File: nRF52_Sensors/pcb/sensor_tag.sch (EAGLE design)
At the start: 6 parts

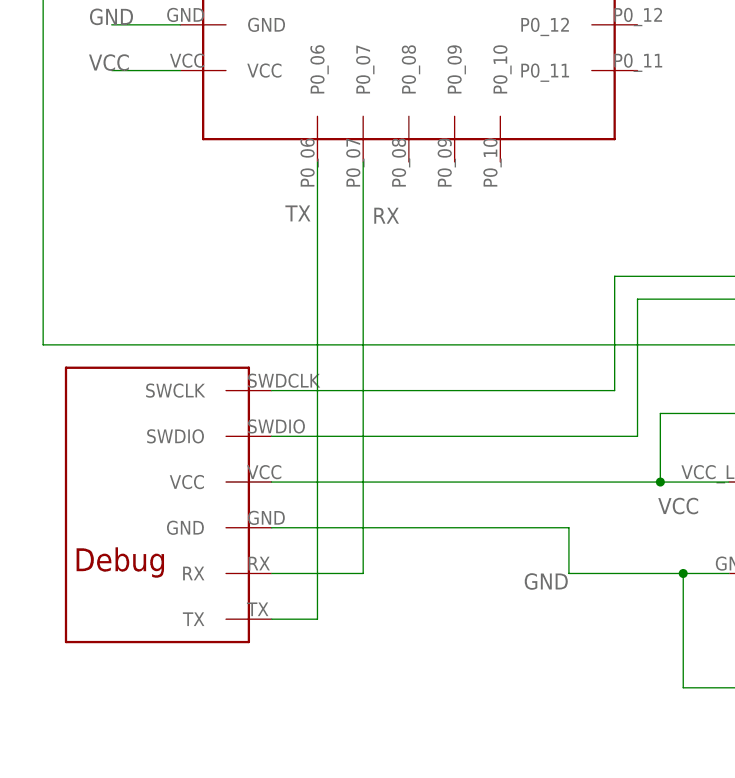
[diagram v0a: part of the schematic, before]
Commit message: fixed board design issues and zip gerber of new order
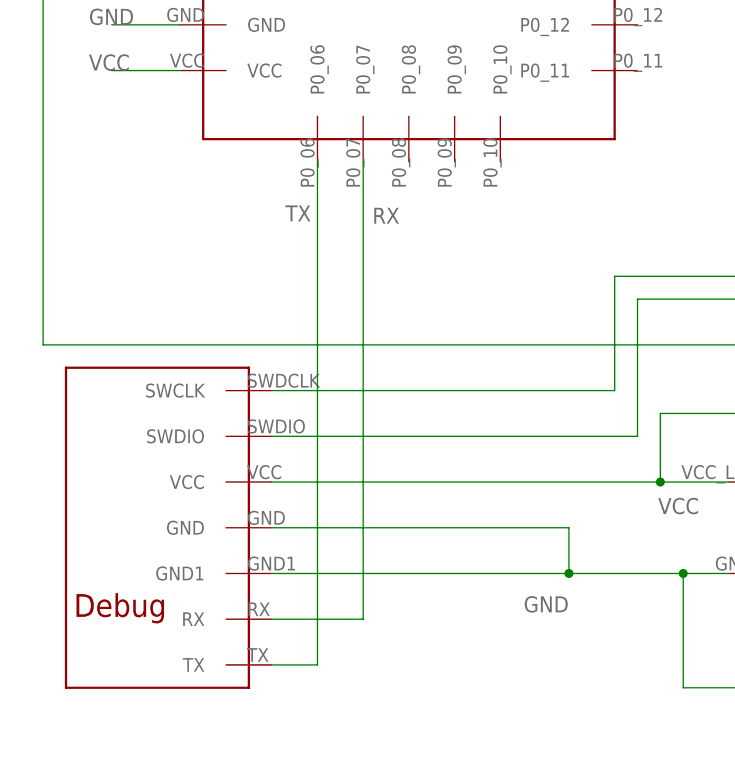
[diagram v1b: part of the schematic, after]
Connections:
- net GND: now also U$5.GND1
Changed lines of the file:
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@@
 <instance part="U$3" gate="G$1" x="-48.26" y="50.8"/>
 <instance part="U$4" gate="G$1" x="-7.62" y="-5.08"/>
-<instance part="U$5" gate="G$1" x="-68.58" y="0" rot="R180"/>
+<instance part="U$5" gate="G$1" x="-68.58" y="-5.08" rot="R180"/>
 <instance part="U$6" gate="G$1" x="33.02" y="-17.78"/>
 </instances>
@@
 <wire x1="-30.48" y1="-5.08" x2="-30.48" y2="-10.16" width="0.1524" layer="91"/>
 <wire x1="-30.48" y1="-10.16" x2="-17.78" y2="-10.16" width="0.1524" layer="91"/>
-<label x="-30.48" y="-10.16" size="1.778" layer="95" rot="R180"/>
+<label x="-30.48" y="-12.7" size="1.778" layer="95" rot="R180"/>
 <wire x1="-17.78" y1="-10.16" x2="-12.7" y2="-10.16" width="0.1524" layer="91"/>
 <wire x1="-17.78" y1="-10.16" x2="-17.78" y2="-22.86" width="0.1524" layer="91"/>
@@
 <wire x1="-17.78" y1="-22.86" x2="20.32" y2="-22.86" width="0.1524" layer="91"/>
 <junction x="-17.78" y="-10.16"/>
+<pinref part="U$5" gate="G$1" pin="GND1"/>
+<wire x1="-63.5" y1="-10.16" x2="-30.48" y2="-10.16" width="0.1524" layer="91"/>
+<junction x="-30.48" y="-10.16"/>
 </segment>
 <segment>
@@
 <pinref part="U$3" gate="G$1" pin="P0_06"/>
 <pinref part="U$5" gate="G$1" pin="TX"/>
-<wire x1="-58.42" y1="35.56" x2="-58.42" y2="-15.24" width="0.1524" layer="91"/>
-<wire x1="-58.42" y1="-15.24" x2="-63.5" y2="-15.24" width="0.1524" layer="91"/>
+<wire x1="-58.42" y1="35.56" x2="-58.42" y2="-20.32" width="0.1524" layer="91"/>
+<wire x1="-58.42" y1="-20.32" x2="-63.5" y2="-20.32" width="0.1524" layer="91"/>
 <label x="-61.976" y="28.956" size="1.778" layer="95"/>
 </segment>
@@
 <segment>
 <pinref part="U$3" gate="G$1" pin="P0_07"/>
-<wire x1="-53.34" y1="35.56" x2="-53.34" y2="-10.16" width="0.1524" layer="91"/>
+<wire x1="-53.34" y1="35.56" x2="-53.34" y2="-15.24" width="0.1524" layer="91"/>
 <pinref part="U$5" gate="G$1" pin="RX"/>
-<wire x1="-53.34" y1="-10.16" x2="-63.5" y2="-10.16" width="0.1524" layer="91"/>
+<wire x1="-53.34" y1="-15.24" x2="-63.5" y2="-15.24" width="0.1524" layer="91"/>
 <label x="-52.324" y="28.702" size="1.778" layer="95"/>
 </segment>
